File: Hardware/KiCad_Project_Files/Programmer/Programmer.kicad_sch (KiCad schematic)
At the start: 24 parts, among them J1 USB_C_Receptacle_USB2.0, J2 R_PI_4, J3 SWD, Q1 FDN335N, U1 MIC5205-3.3YM5, U2 ATSAMD21G18A-A, Y1 32.876

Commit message: schem save
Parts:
- gave numbers to parts that had none: 1
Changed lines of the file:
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@@
   (symbol (lib_id "Device:Fuse_Small") (at 91.44 92.71 0) (unit 1)
     (in_bom yes) (on_board yes)
-    (property "Reference" "F?" (id 0) (at 92.075 86.995 0))
+    (property "Reference" "F1" (id 0) (at 92.075 86.995 0))
     (property "Value" "Fuse_Small" (id 1) (at 92.075 89.535 0))
     (property "Footprint" "Fuse:Fuse_0603_1608Metric_Castellated" (id 2) (at 91.44 92.71 0)
@@
     )
     (path "/986182ae-d382-4bf4-9888-5efaead4ed1d"
-      (reference "F?") (unit 1)
+      (reference "F1") (unit 1)
     )
     (path "/a41027ad-f56a-495d-82be-a54990a7da38"

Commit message: layout init
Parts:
- added R? (x2): 330Ω, Resistor_SMD:R_0603_1608Metric, symbol Device:R_Small_US
- added SW?: START, Button_Switch_SMD:SW_SPST_TL3342, symbol Switch:SW_Push_45deg
- added SW?: MODE, Button_Switch_SMD:SW_SPST_TL3342, symbol Switch:SW_Push_45deg
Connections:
- net +3V3: now also R?.1, R?.1
- net GND: now also SW?.1, SW?.1
- net IO2 renamed SDA
- net IO3 renamed SCL
- net IO5 renamed START
- net START: now also R?.2, SW?.2
- net IO6 renamed MODE
- net MODE: now also R?.2, SW?.2
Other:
- moved on the sheet: C3, C4, C5, C6, C7, C8, C9, D1, D2, F1, J1, R2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

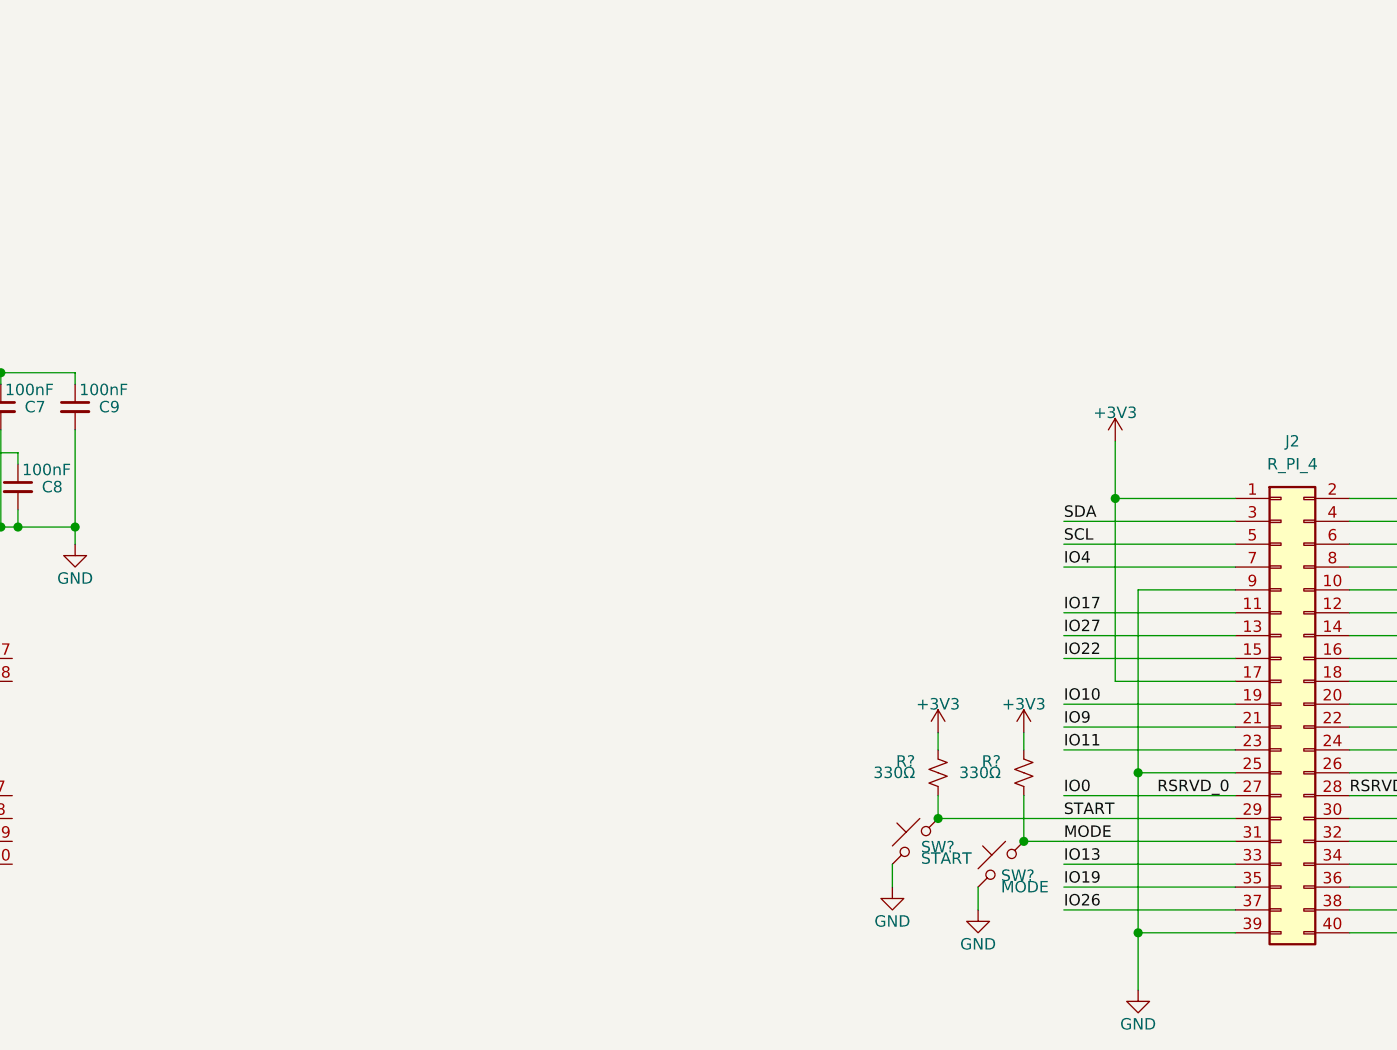
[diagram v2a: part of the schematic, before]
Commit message: added oled
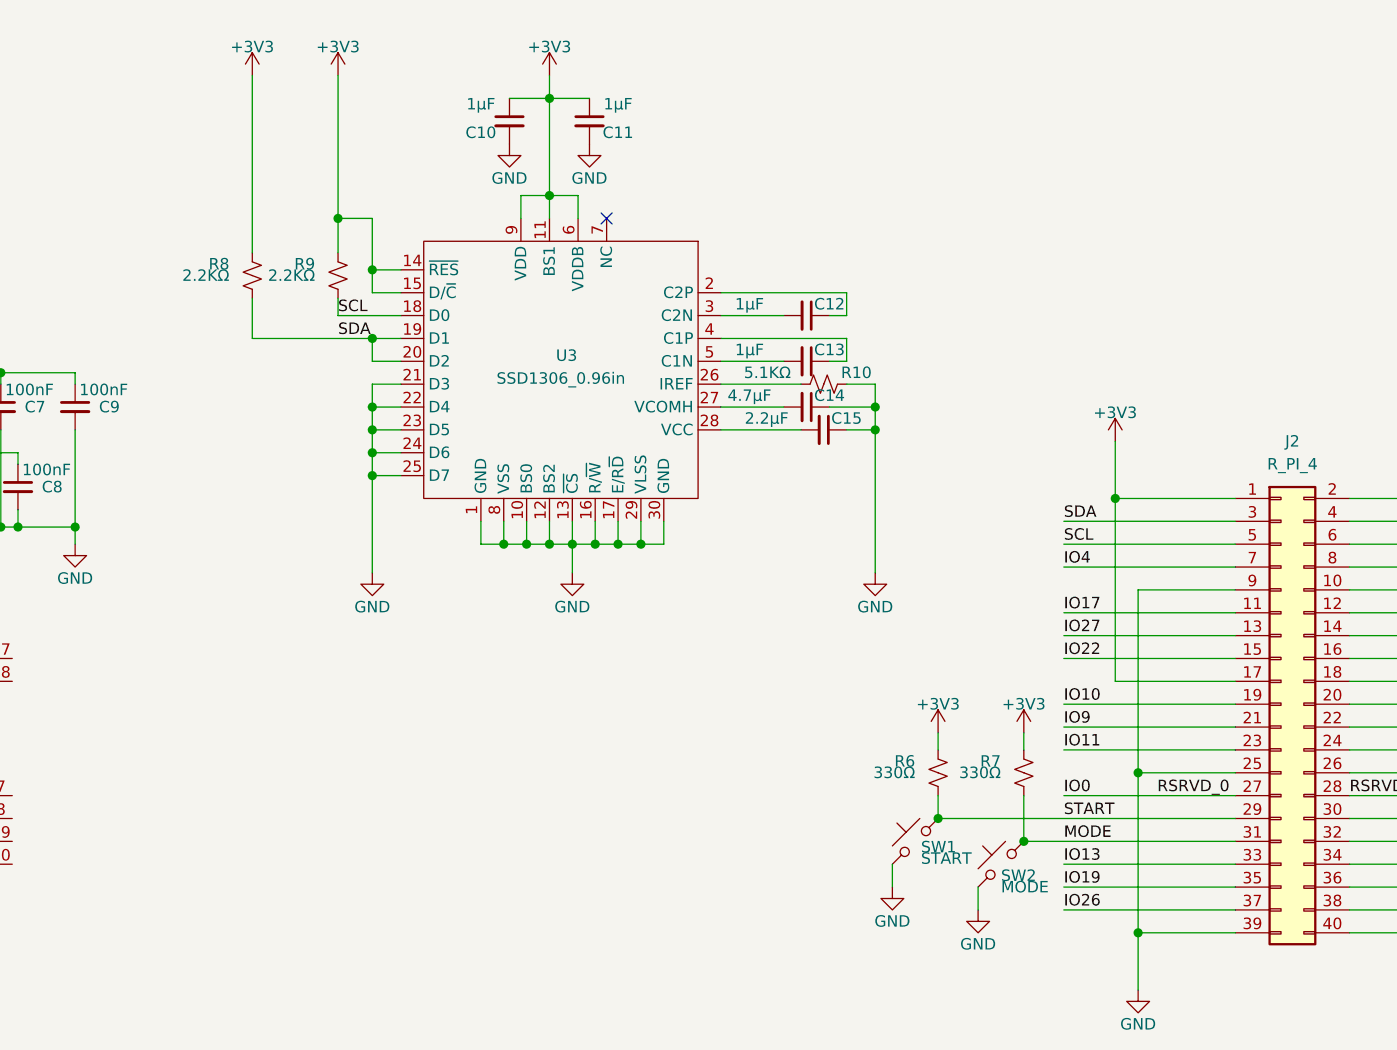
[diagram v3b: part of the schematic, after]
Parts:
- added C10, C11, C12, C13: 1µF, Capacitor_SMD:C_0603_1608Metric, symbol Device:C_Small
- added C14: 4.7µF, Capacitor_SMD:C_0603_1608Metric, symbol Device:C_Small
- added C15: 2.2µF, Capacitor_SMD:C_0603_1608Metric, symbol Device:C_Small
- added R10: 5.1KΩ, Resistor_SMD:R_0603_1608Metric, symbol Device:R_Small_US
- added R8, R9: 2.2KΩ, Resistor_SMD:R_0603_1608Metric, symbol Device:R_Small_US
- added U3: SSD1306_0.96in, Custom_Displays:SSD1306_0.96in, symbol Custom_Displays:SSD1306_0.96in
- gave numbers to parts that had none: 4
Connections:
- net +3V3: now also C10.1, C11.1, R8.1, R9.1, U3.11 (BS1), U3.14 (~RES), U3.15 (D/~C), U3.6 (VDDB), U3.9 (VDD)
- net GND: now also C10.2, C11.2, C14.1, C15.1, R10.2, U3.1 (GND), U3.10 (BS0), U3.12 (BS2), U3.13 (~CS), U3.16 (R/~W), U3.17 (E/R~D), U3.21 (D3), U3.22 (D4), U3.23 (D5), U3.24 (D6), U3.25 (D7), U3.29 (VLSS), U3.30 (GND), U3.8 (VSS)
- net SCL: now also R9.2, U3.18 (D0)
- net SDA: now also R8.2, U3.19 (D1), U3.20 (D2)
- new net: C12.1, U3.2 (C2P)
- new net: R10.1, U3.26 (IREF)
- new net: C14.2, U3.27 (VCOMH)
- new net: C15.2, U3.28 (VCC)
- new net: C12.2, U3.3 (C2N)
- new net: C13.1, U3.4 (C1P)
- new net: C13.2, U3.5 (C1N)
- no-connect marks 7 -> 8
